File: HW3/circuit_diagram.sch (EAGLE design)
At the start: 11 parts

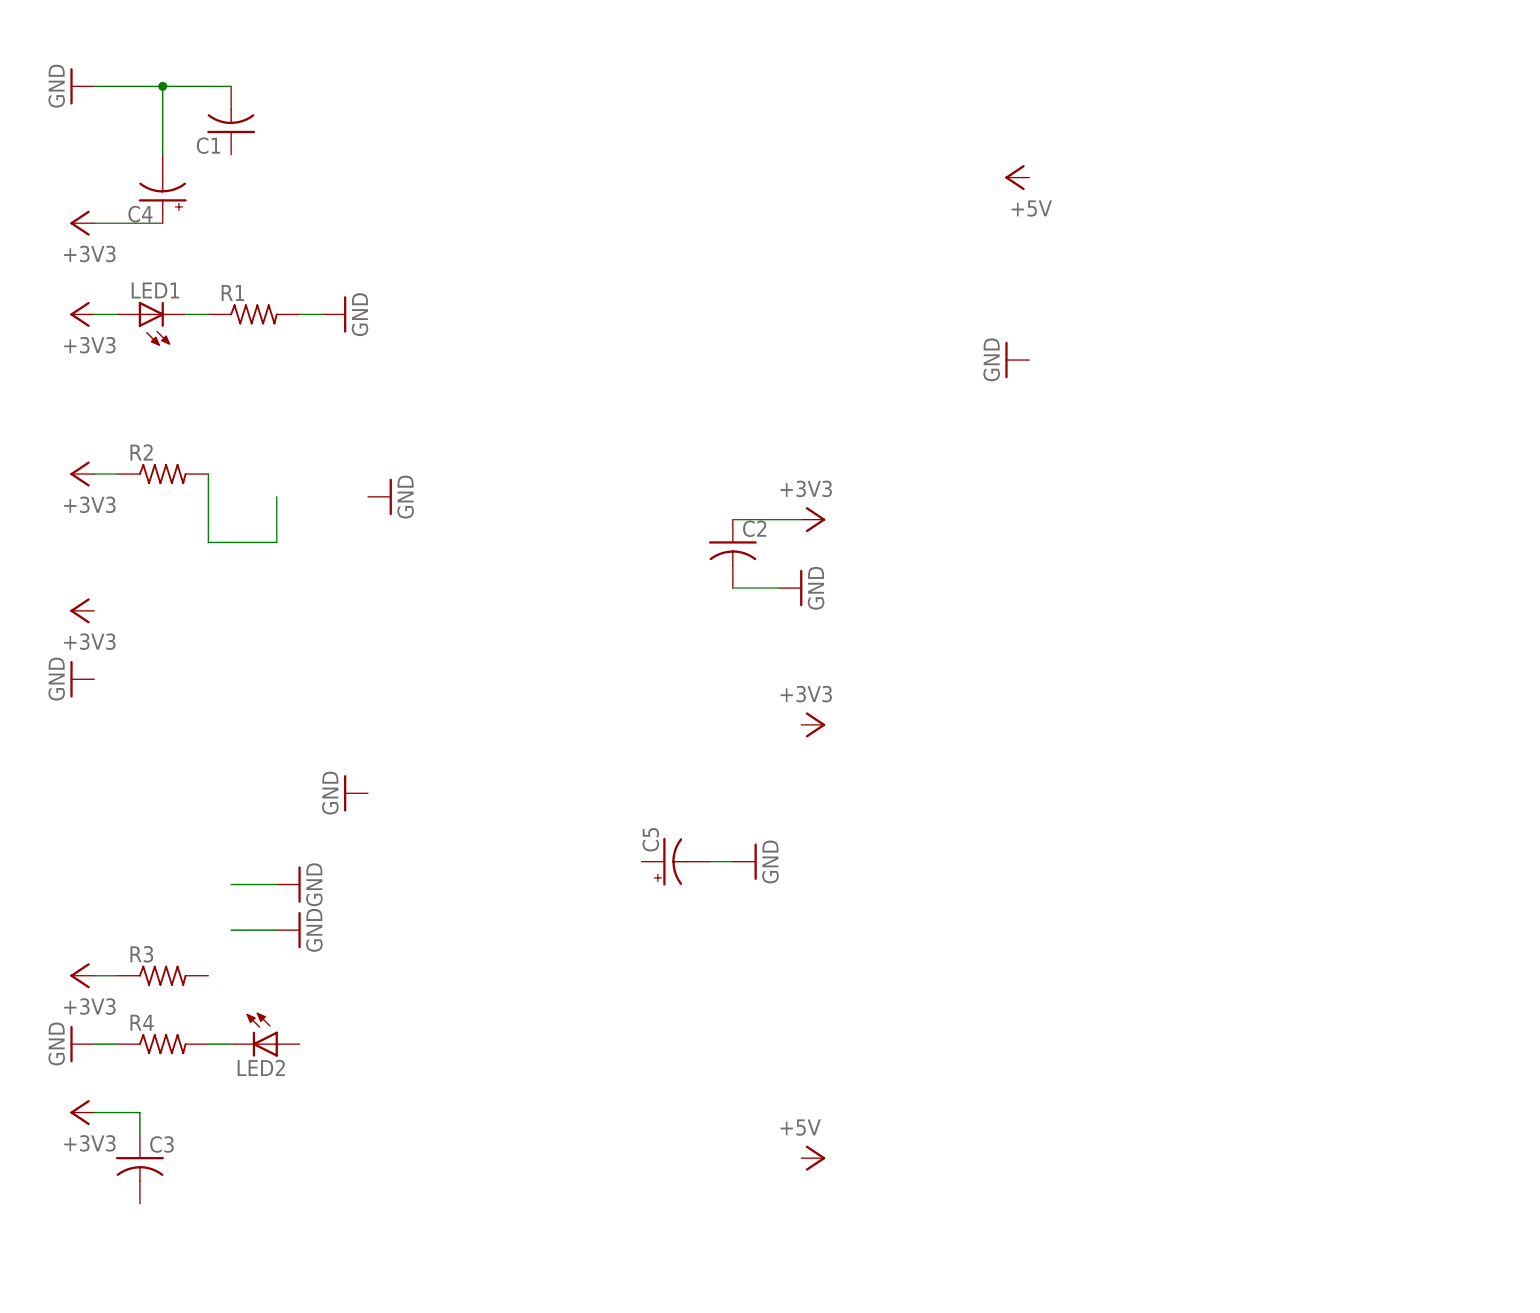
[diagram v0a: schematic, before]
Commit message: Added PIC32
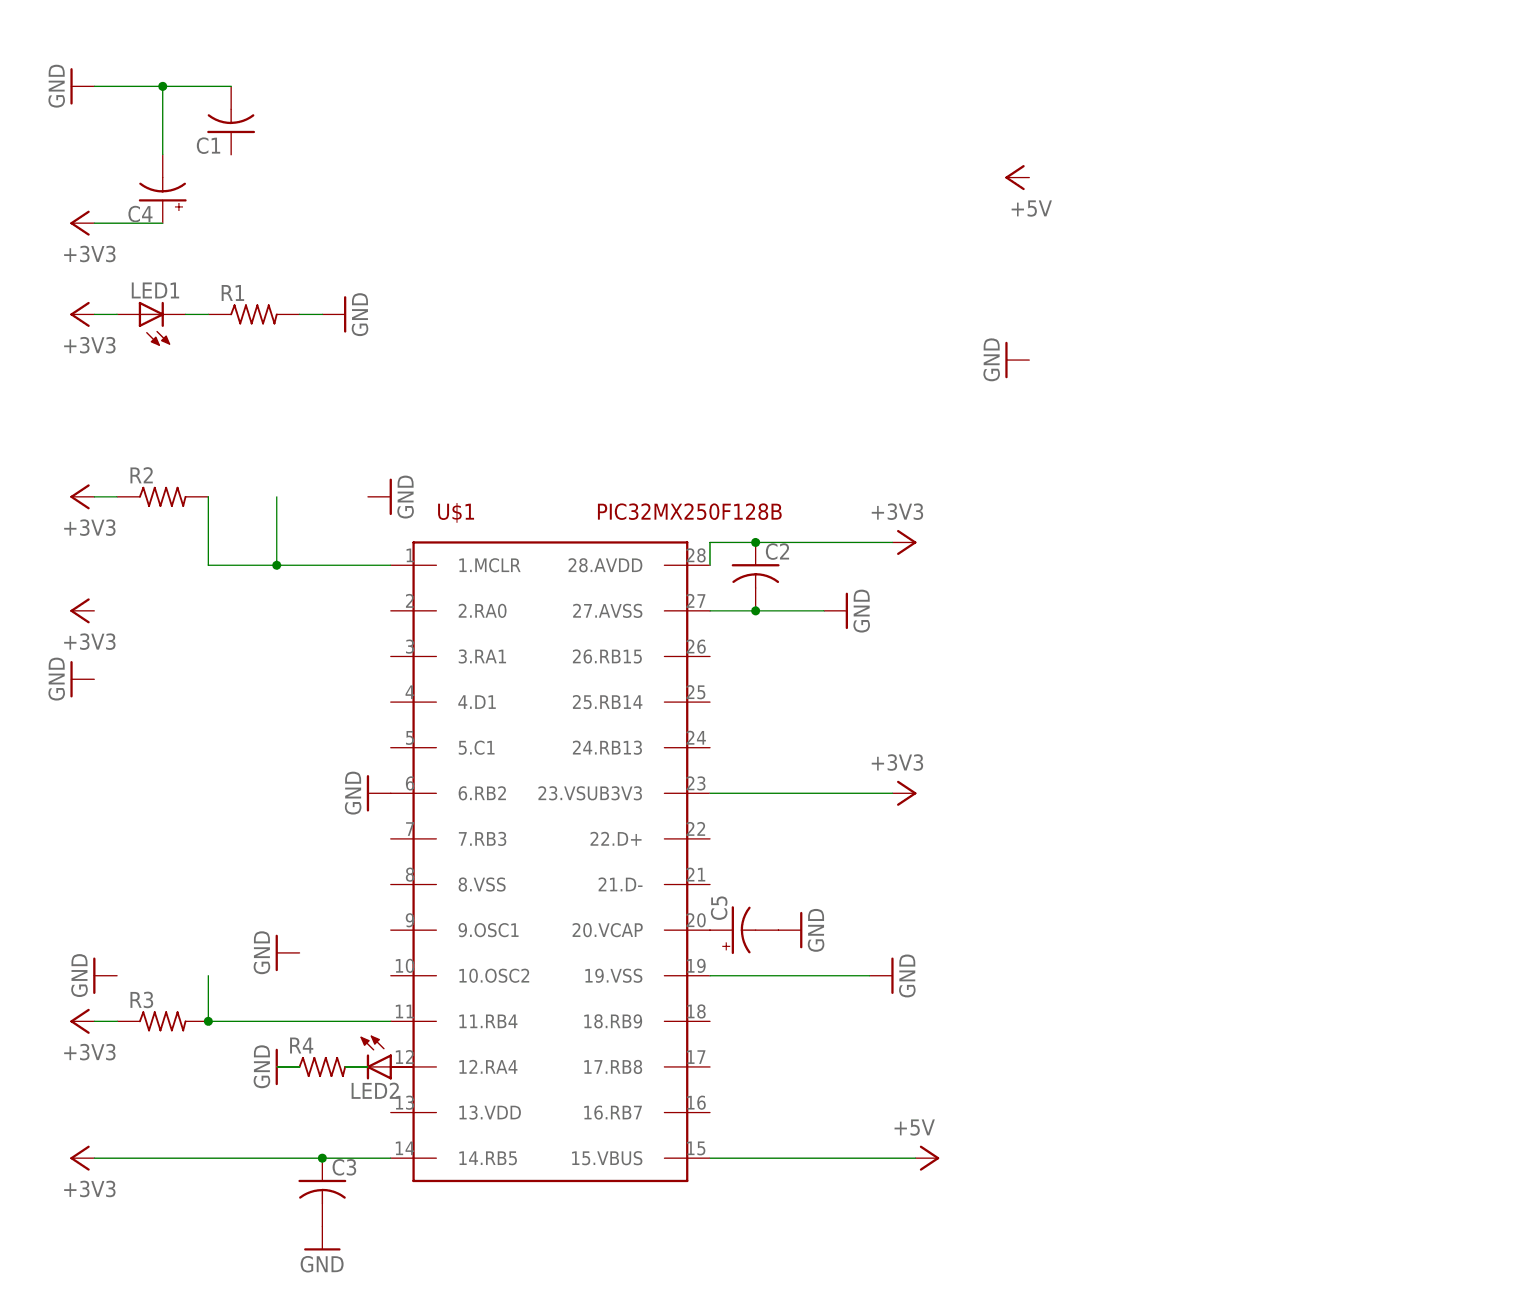
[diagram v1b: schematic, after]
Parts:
- added U$1: PIC32MX250F128B, PIC32MX250F128B:PIC32MX250F128B
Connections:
- new net +5V: U$1.15.VBUS
- new net N$4: C5.+, U$1.20.VCAP
- new net N$5: R3.2, U$1.11.RB4
- net +3V3: now also U$1.14.RB5, U$1.23.VSUB3V3, U$1.28.AVDD
- net GND: now also C3.2, U$1.19.VSS, U$1.27.AVSS, U$1.6.RB2
- net N$3: now also U$1.1.MCLR
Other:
- moved on the sheet: C2, C3, C5, LED2, R2, R3, R4
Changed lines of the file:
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@@
 <part name="C4" library="resistor" library_urn="urn:adsk.eagle:library:348" deviceset="CPOL-US" device="CT3216" package3d_urn="urn:adsk.eagle:package:25799/1"/>
 <part name="C5" library="resistor" library_urn="urn:adsk.eagle:library:348" deviceset="CPOL-US" device="CT3216" package3d_urn="urn:adsk.eagle:package:25799/1"/>
+<part name="U$1" library="PIC32MX250F128B" deviceset="PIC32MX250F128B" device=""/>
+<part name="GND12" library="supply1" library_urn="urn:adsk.eagle:library:371" deviceset="GND" device=""/>
+<part name="GND13" library="supply1" library_urn="urn:adsk.eagle:library:371" deviceset="GND" device=""/>
 </parts>
 <sheets>
@@
 <instances>
 <instance part="R1" gate="G$1" x="-22.86" y="33.02"/>
-<instance part="R2" gate="G$1" x="-33.02" y="15.24"/>
-<instance part="R3" gate="G$1" x="-33.02" y="-40.64"/>
-<instance part="R4" gate="G$1" x="-33.02" y="-48.26"/>
+<instance part="R2" gate="G$1" x="-33.02" y="12.7"/>
+<instance part="R3" gate="G$1" x="-33.02" y="-45.72"/>
+<instance part="R4" gate="G$1" x="-15.24" y="-50.8"/>
 <instance part="LED1" gate="G$1" x="-35.56" y="33.02" rot="R90"/>
-<instance part="LED2" gate="G$1" x="-20.32" y="-48.26" rot="R270"/>
+<instance part="LED2" gate="G$1" x="-7.62" y="-50.8" rot="R270"/>
 <instance part="+3V1" gate="G$1" x="-43.18" y="33.02" rot="R90"/>
-<instance part="+3V2" gate="G$1" x="-43.18" y="15.24" rot="R90"/>
+<instance part="+3V2" gate="G$1" x="-43.18" y="12.7" rot="R90"/>
 <instance part="+3V3" gate="G$1" x="-43.18" y="0" rot="R90"/>
-<instance part="+3V4" gate="G$1" x="-43.18" y="-40.64" rot="R90"/>
-<instance part="+3V5" gate="G$1" x="-43.18" y="-55.88" rot="R90"/>
-<instance part="+3V6" gate="G$1" x="40.64" y="10.16" rot="R270"/>
-<instance part="+3V7" gate="G$1" x="40.64" y="-12.7" rot="R270"/>
+<instance part="+3V4" gate="G$1" x="-43.18" y="-45.72" rot="R90"/>
+<instance part="+3V5" gate="G$1" x="-43.18" y="-60.96" rot="R90"/>
+<instance part="+3V6" gate="G$1" x="50.8" y="7.62" rot="R270"/>
+<instance part="+3V7" gate="G$1" x="50.8" y="-20.32" rot="R270"/>
 <instance part="+3V8" gate="G$1" x="-43.18" y="43.18" rot="R90"/>
 <instance part="GND1" gate="1" x="-43.18" y="58.42" rot="R270"/>
 <instance part="GND2" gate="1" x="-12.7" y="33.02" rot="R90"/>
 <instance part="GND3" gate="1" x="-7.62" y="12.7" rot="R90"/>
-<instance part="GND4" gate="1" x="-17.78" y="-30.48" rot="R90"/>
-<instance part="GND5" gate="1" x="-17.78" y="-35.56" rot="R90"/>
-<instance part="GND6" gate="1" x="38.1" y="2.54" rot="R90"/>
-<instance part="GND7" gate="1" x="33.02" y="-27.94" rot="R90"/>
+<instance part="GND4" gate="1" x="-20.32" y="-38.1" rot="R270"/>
+<instance part="GND5" gate="1" x="-40.64" y="-40.64" rot="R270"/>
+<instance part="GND6" gate="1" x="43.18" y="0" rot="R90"/>
+<instance part="GND7" gate="1" x="38.1" y="-35.56" rot="R90"/>
 <instance part="GND8" gate="1" x="60.96" y="27.94" rot="R270"/>
-<instance part="GND9" gate="1" x="-12.7" y="-20.32" rot="R270"/>
-<instance part="GND10" gate="1" x="-43.18" y="-48.26" rot="R270"/>
+<instance part="GND9" gate="1" x="-10.16" y="-20.32" rot="R270"/>
+<instance part="GND10" gate="1" x="-20.32" y="-50.8" rot="R270"/>
 <instance part="GND11" gate="1" x="-43.18" y="-7.62" rot="R270"/>
-<instance part="P+1" gate="1" x="40.64" y="-60.96" rot="R270"/>
+<instance part="P+1" gate="1" x="53.34" y="-60.96" rot="R270"/>
 <instance part="P+2" gate="1" x="60.96" y="48.26" rot="R90"/>
 <instance part="C1" gate="G$1" x="-25.4" y="53.34" rot="R180"/>
-<instance part="C2" gate="G$1" x="30.48" y="7.62"/>
-<instance part="C3" gate="G$1" x="-35.56" y="-60.96"/>
+<instance part="C2" gate="G$1" x="33.02" y="5.08"/>
+<instance part="C3" gate="G$1" x="-15.24" y="-63.5"/>
 <instance part="C4" gate="G$1" x="-33.02" y="45.72" rot="R180"/>
-<instance part="C5" gate="G$1" x="22.86" y="-27.94" rot="R90"/>
+<instance part="C5" gate="G$1" x="30.48" y="-35.56" rot="R90"/>
+<instance part="U$1" gate="G$1" x="10.16" y="-25.4"/>
+<instance part="GND12" gate="1" x="48.26" y="-40.64" rot="R90"/>
+<instance part="GND13" gate="1" x="-15.24" y="-71.12"/>
 </instances>
 <busses>
@@
 <pinref part="+3V2" gate="G$1" pin="+3V3"/>
 <pinref part="R2" gate="G$1" pin="1"/>
-<wire x1="-40.64" y1="15.24" x2="-38.1" y2="15.24" width="0.1524" layer="91"/>
+<wire x1="-40.64" y1="12.7" x2="-38.1" y2="12.7" width="0.1524" layer="91"/>
 </segment>
 <segment>
 <pinref part="+3V5" gate="G$1" pin="+3V3"/>
-<wire x1="-40.64" y1="-55.88" x2="-35.56" y2="-55.88" width="0.1524" layer="91"/>
 <pinref part="C3" gate="G$1" pin="1"/>
-<wire x1="-35.56" y1="-55.88" x2="-35.56" y2="-58.42" width="0.1524" layer="91"/>
+<wire x1="-40.64" y1="-60.96" x2="-15.24" y2="-60.96" width="0.1524" layer="91"/>
+<pinref part="U$1" gate="G$1" pin="14.RB5"/>
+<wire x1="-15.24" y1="-60.96" x2="-7.62" y2="-60.96" width="0.1524" layer="91"/>
+<junction x="-15.24" y="-60.96"/>
 </segment>
 <segment>
 <pinref part="C2" gate="G$1" pin="1"/>
 <pinref part="+3V6" gate="G$1" pin="+3V3"/>
-<wire x1="30.48" y1="10.16" x2="38.1" y2="10.16" width="0.1524" layer="91"/>
+<wire x1="33.02" y1="7.62" x2="48.26" y2="7.62" width="0.1524" layer="91"/>
+<pinref part="U$1" gate="G$1" pin="28.AVDD"/>
+<wire x1="27.94" y1="5.08" x2="27.94" y2="7.62" width="0.1524" layer="91"/>
+<wire x1="27.94" y1="7.62" x2="33.02" y2="7.62" width="0.1524" layer="91"/>
+<junction x="33.02" y="7.62"/>
 </segment>
 <segment>
 <pinref part="+3V4" gate="G$1" pin="+3V3"/>
 <pinref part="R3" gate="G$1" pin="1"/>
-<wire x1="-40.64" y1="-40.64" x2="-38.1" y2="-40.64" width="0.1524" layer="91"/>
+<wire x1="-40.64" y1="-45.72" x2="-38.1" y2="-45.72" width="0.1524" layer="91"/>
+</segment>
+<segment>
+<pinref part="U$1" gate="G$1" pin="23.VSUB3V3"/>
+<pinref part="+3V7" gate="G$1" pin="+3V3"/>
+<wire x1="27.94" y1="-20.32" x2="48.26" y2="-20.32" width="0.1524" layer="91"/>
 </segment>
 </net>
@@
 <pinref part="GND10" gate="1" pin="GND"/>
 <pinref part="R4" gate="G$1" pin="1"/>
-<wire x1="-40.64" y1="-48.26" x2="-38.1" y2="-48.26" width="0.1524" layer="91"/>
+<wire x1="-17.78" y1="-50.8" x2="-20.32" y2="-50.8" width="0.1524" layer="91"/>
 </segment>
 <segment>
 <pinref part="C5" gate="G$1" pin="-"/>
 <pinref part="GND7" gate="1" pin="GND"/>
-<wire x1="27.94" y1="-27.94" x2="30.48" y2="-27.94" width="0.1524" layer="91"/>
 </segment>
 <segment>
 <pinref part="C2" gate="G$1" pin="2"/>
 <pinref part="GND6" gate="1" pin="GND"/>
-<wire x1="30.48" y1="2.54" x2="35.56" y2="2.54" width="0.1524" layer="91"/>
+<wire x1="33.02" y1="0" x2="40.64" y2="0" width="0.1524" layer="91"/>
+<pinref part="U$1" gate="G$1" pin="27.AVSS"/>
+<wire x1="27.94" y1="0" x2="33.02" y2="0" width="0.1524" layer="91"/>
+<junction x="33.02" y="0"/>
 </segment>
 <segment>
@@
 </segment>
 <segment>
-<pinref part="GND5" gate="1" pin="GND"/>
-<wire x1="-20.32" y1="-35.56" x2="-25.4" y2="-35.56" width="0.1524" layer="91"/>
+<pinref part="C3" gate="G$1" pin="2"/>
+<pinref part="GND13" gate="1" pin="GND"/>
 </segment>
 <segment>
-<pinref part="GND4" gate="1" pin="GND"/>
-<wire x1="-20.32" y1="-30.48" x2="-25.4" y2="-30.48" width="0.1524" layer="91"/>
+<pinref part="U$1" gate="G$1" pin="6.RB2"/>
+<pinref part="GND9" gate="1" pin="GND"/>
+</segment>
+<segment>
+<pinref part="U$1" gate="G$1" pin="19.VSS"/>
+<pinref part="GND12" gate="1" pin="GND"/>
+<wire x1="27.94" y1="-40.64" x2="45.72" y2="-40.64" width="0.1524" layer="91"/>
 </segment>
 </net>
@@
 <pinref part="R4" gate="G$1" pin="2"/>
 <pinref part="LED2" gate="G$1" pin="C"/>
-<wire x1="-27.94" y1="-48.26" x2="-25.4" y2="-48.26" width="0.1524" layer="91"/>
+<wire x1="-10.16" y1="-50.8" x2="-12.7" y2="-50.8" width="0.1524" layer="91"/>
 </segment>
 </net>
@@
 <segment>
 <pinref part="R2" gate="G$1" pin="2"/>
-<wire x1="-27.94" y1="15.24" x2="-27.94" y2="7.62" width="0.1524" layer="91"/>
-<wire x1="-27.94" y1="7.62" x2="-20.32" y2="7.62" width="0.1524" layer="91"/>
-<wire x1="-20.32" y1="7.62" x2="-20.32" y2="12.7" width="0.1524" layer="91"/>
+<wire x1="-27.94" y1="12.7" x2="-27.94" y2="5.08" width="0.1524" layer="91"/>
+<pinref part="U$1" gate="G$1" pin="1.MCLR"/>
+<wire x1="-27.94" y1="5.08" x2="-20.32" y2="5.08" width="0.1524" layer="91"/>
+<wire x1="-20.32" y1="5.08" x2="-7.62" y2="5.08" width="0.1524" layer="91"/>
+<wire x1="-20.32" y1="5.08" x2="-20.32" y2="12.7" width="0.1524" layer="91"/>
+<junction x="-20.32" y="5.08"/>
 </segment>
 </net>
+<net name="N$4" class="0">
+<segment>
+<pinref part="U$1" gate="G$1" pin="20.VCAP"/>
+<pinref part="C5" gate="G$1" pin="+"/>
+</segment>
+</net>
+<net name="+5V" class="0">
+<segment>
+<pinref part="U$1" gate="G$1" pin="15.VBUS"/>
+<pinref part="P+1" gate="1" pin="+5V"/>
+<wire x1="27.94" y1="-60.96" x2="50.8" y2="-60.96" width="0.1524" layer="91"/>
+</segment>
+</net>
+<net name="N$5" class="0">
+<segment>
+<pinref part="R3" gate="G$1" pin="2"/>
+<pinref part="U$1" gate="G$1" pin="11.RB4"/>
+<wire x1="-27.94" y1="-45.72" x2="-7.62" y2="-45.72" width="0.1524" layer="91"/>
+<wire x1="-27.94" y1="-45.72" x2="-27.94" y2="-40.64" width="0.1524" layer="91"/>
+<junction x="-27.94" y="-45.72"/>
+</segment>
+</net>

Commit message: Added USB
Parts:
- added U$2, U$3: PUSH_BUTTON_SPST-NO, PUSH_BUTTON:PUSH_BUTTON_SPST-NO
- added U$4: USB_MINI, usb_conn:USB_MINI
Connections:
- new net N$6: U$1.22.D+, U$4.D+
- new net N$7: U$1.21.D-, U$4.D-
- net +5V: now also U$4.VBUS
- net GND: now also U$2.2, U$3.1, U$4.GND
- net N$3: now also U$2.1
- net N$5: now also U$3.2
